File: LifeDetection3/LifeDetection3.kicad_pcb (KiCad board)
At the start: 4 copper layers, 19 parts, among them J1 Power, J13 XT60PW-M, J2 PWM, J3 Analog, J4 PWM, J5 Analog, J6 Communication, J7 Digital

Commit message: lil changes
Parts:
- added ?: , , F.Cu at (196.5, 97.5)
- added ?: , , F.Cu at (163.5, 92.4)
- added ?: , , F.Cu at (114.0, 97.5)
- added ?: , , F.Cu at (115.2, 49.2)
- added P13: CONN_01X01, Socket_Arduino_Mega:Arduino_1pin, F.Cu at (190.2, 49.2)
- moved J13 23.0 mm to (102.5, 46.7)
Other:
- board outline added: 105 x 88.1 mm
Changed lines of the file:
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@@
     )
+  )
+  (footprint "" (layer "F.Cu")
+    (at 196.52 97.485)
+    (fp_text reference "" (at 0 0) (layer "F.SilkS")
+      (effects (font (size 1.27 1.27) (thickness 0.15)))
+    )
+    (fp_text value "" (at 0 0) (layer "F.SilkS")
+      (effects (font (size 1.27 1.27) (thickness 0.15)))
+    )
+    (pad "1" thru_hole circle locked (at 0 0) (size 4.064 4.064) (drill 3.048) (layers *.Mask "F.Cu" "In1.Cu" "In2.Cu" "B.Cu" "F.SilkS")
+      (pinfunction "Pin_1") (pintype "passive+no_connect"))
   )
   (footprint "Connector_PinSocket_2.54mm:PinSocket_1x08_P2.54mm_Vertical" (layer "F.Cu")
@@
     )
   )
+  (footprint "" (layer "F.Cu")
+    (at 163.5 92.38)
+    (fp_text reference "" (at 0 0) (layer "F.SilkS")
+      (effects (font (size 1.27 1.27) (thickness 0.15)))
+    )
+    (fp_text value "" (at 0 0) (layer "F.SilkS")
+      (effects (font (size 1.27 1.27) (thickness 0.15)))
+    )
+    (pad "1" thru_hole circle locked (at 0 0) (size 4.064 4.064) (drill 3.048) (layers *.Mask "F.Cu" "In1.Cu" "In2.Cu" "B.Cu" "F.SilkS")
+      (pinfunction "Pin_1") (pintype "passive+no_connect"))
+  )
   (footprint "XT60:AMASS_XT60PW-M" (layer "F.Cu")
-    (at 105.08 69.52 90)
+    (at 102.54 46.66 90)
     (property "MANUFACTURER" "AMASS")
     (property "MAXIMUM_PACKAGE_HEIGHT" "8.4 mm")
@@
     )
   )
+  (footprint "" (layer "F.Cu")
+    (at 113.97 97.485)
+    (fp_text reference "" (at 0 0) (layer "F.SilkS")
+      (effects (font (size 1.27 1.27) (thickness 0.15)))
+    )
+    (fp_text value "" (at 0 0) (layer "F.SilkS")
+      (effects (font (size 1.27 1.27) (thickness 0.15)))
+    )
+    (pad "1" thru_hole circle locked (at 0 0) (size 4.064 4.064) (drill 3.048) (layers *.Mask "F.Cu" "In1.Cu" "In2.Cu" "B.Cu" "F.SilkS")
+      (pinfunction "Pin_1") (pintype "passive+no_connect"))
+  )
   (footprint "Connector_PinSocket_2.54mm:PinSocket_1x08_P2.54mm_Vertical" (layer "F.Cu")
     (at 171.12 64.44)
@@
     )
   )
+  (footprint "Socket_Arduino_Mega:Arduino_1pin" (layer "F.Cu")
+    (at 190.17 49.225)
+    (descr "module 1 pin (ou trou mecanique de percage)")
+    (tags "DEV")
+    (property "Sheetfile" "ArmSheildR2.kicad_sch")
+    (property "Sheetname" "")
+    (attr through_hole)
+    (fp_text reference "P13" (at 0 -3.048) (layer "F.SilkS") hide
+      (effects (font (size 1 1) (thickness 0.15)))
+    )
+    (fp_text value "CONN_01X01" (at 0 2.794) (layer "F.Fab") hide
+      (effects (font (size 1 1) (thickness 0.15)))
+    )
+    (fp_circle (center 0 0) (end 0 -2.286) (layer "F.SilkS") (width 0.15) (fill none))
+    (pad "1" thru_hole circle locked (at 0 0) (size 4.064 4.064) (drill 3.048) (layers *.Mask "F.Cu" "In1.Cu" "In2.Cu" "B.Cu" "F.SilkS")
+      (pinfunction "Pin_1") (pintype "passive+no_connect"))
+  )
   (footprint "Connector_PinSocket_2.54mm:PinSocket_1x08_P2.54mm_Vertical" (layer "F.Cu")
     (at 155.88 64.44)
@@
     )
   )
-  (gr_rect (start 201.6 110.16) (end 89.84 26.34) (layer "F.Cu") (width 0.15) (fill none))
+  (footprint "" (layer "F.Cu")
+    (at 115.24 49.225)
+    (fp_text reference "" (at 0 0) (layer "F.SilkS")
+      (effects (font (size 1.27 1.27) (thickness 0.15)))
+    )
+    (fp_text value "" (at 0 0) (layer "F.SilkS")
+      (effects (font (size 1.27 1.27) (thickness 0.15)))
+    )
+    (pad "1" thru_hole circle locked (at 0 0) (size 4.064 4.064) (drill 3.048) (layers *.Mask "F.Cu" "In1.Cu" "In2.Cu" "B.Cu" "F.SilkS")
+      (pinfunction "Pin_1") (pintype "passive+no_connect"))
+  )
+  (gr_line (start 94.62 57.02) (end 94.62 46.02) (layer "Edge.Cuts") (width 0.15))
+  (gr_line (start 101.62 23.8) (end 189.62 23.8) (layer "Edge.Cuts") (width 0.15))
+  (gr_arc (start 94.62 80.02) (mid 95.205786 78.605786) (end 96.62 78.02) (layer "Edge.Cuts") (width 0.15))
+  (gr_arc (start 98.62 61.02) (mid 95.791573 59.848427) (end 94.62 57.02) (layer "Edge.Cuts") (width 0.15))
+  (gr_arc (start 199.62 105.917359) (mid 197.862641 110.16) (end 193.62 111.917359) (layer "Edge.Cuts") (width 0.15))
+  (gr_line (start 105.62 61.02) (end 98.62 61.02) (layer "Edge.Cuts") (width 0.15))
+  (gr_line (start 191.44 23.8) (end 189.62 23.8) (layer "Edge.Cuts") (width 0.15))
+  (gr_line (start 199.62 105.917359) (end 199.62 33.02) (layer "Edge.Cuts") (width 0.15))
+  (gr_arc (start 94.62 31.42) (mid 96.643931 26.254034) (end 101.62 23.8) (layer "Edge.Cuts") (width 0.15))
+  (gr_arc (start 101.62 111.917359) (mid 96.670253 109.867106) (end 94.62 104.917359) (layer "Edge.Cuts") (width 0.15))
+  (gr_line (start 199.62 31.42) (end 199.62 33.02) (layer "Edge.Cuts") (width 0.15))
+  (gr_line (start 94.62 46.02) (end 94.62 31.42) (layer "Edge.Cuts") (width 0.15))
+  (gr_arc (start 105.62 61.02) (mid 107.034214 61.605786) (end 107.62 63.02) (layer "Edge.Cuts") (width 0.15))
+  (gr_arc (start 107.62 76.02) (mid 107.034214 77.434214) (end 105.62 78.02) (layer "Edge.Cuts") (width 0.15))
+  (gr_line (start 107.62 63.02) (end 107.62 76.02) (layer "Edge.Cuts") (width 0.15))
+  (gr_line (start 105.62 78.02) (end 96.62 78.02) (layer "Edge.Cuts") (width 0.15))
+  (gr_line (start 94.62 80.02) (end 94.62 104.917359) (layer "Edge.Cuts") (width 0.15))
+  (gr_arc (start 191.44 23.8) (mid 196.911013 26.127496) (end 199.62 31.42) (layer "Edge.Cuts") (width 0.15))
+  (gr_line (start 193.62 111.917359) (end 101.62 111.917359) (layer "Edge.Cuts") (width 0.15))
   (segment (start 171.12 69.52) (end 158.42 82.22) (width 0.25) (layer "F.Cu") (net 1))
   (segment (start 158.42 82.22) (end 155.88 82.22) (width 0.25) (layer "F.Cu") (net 1))

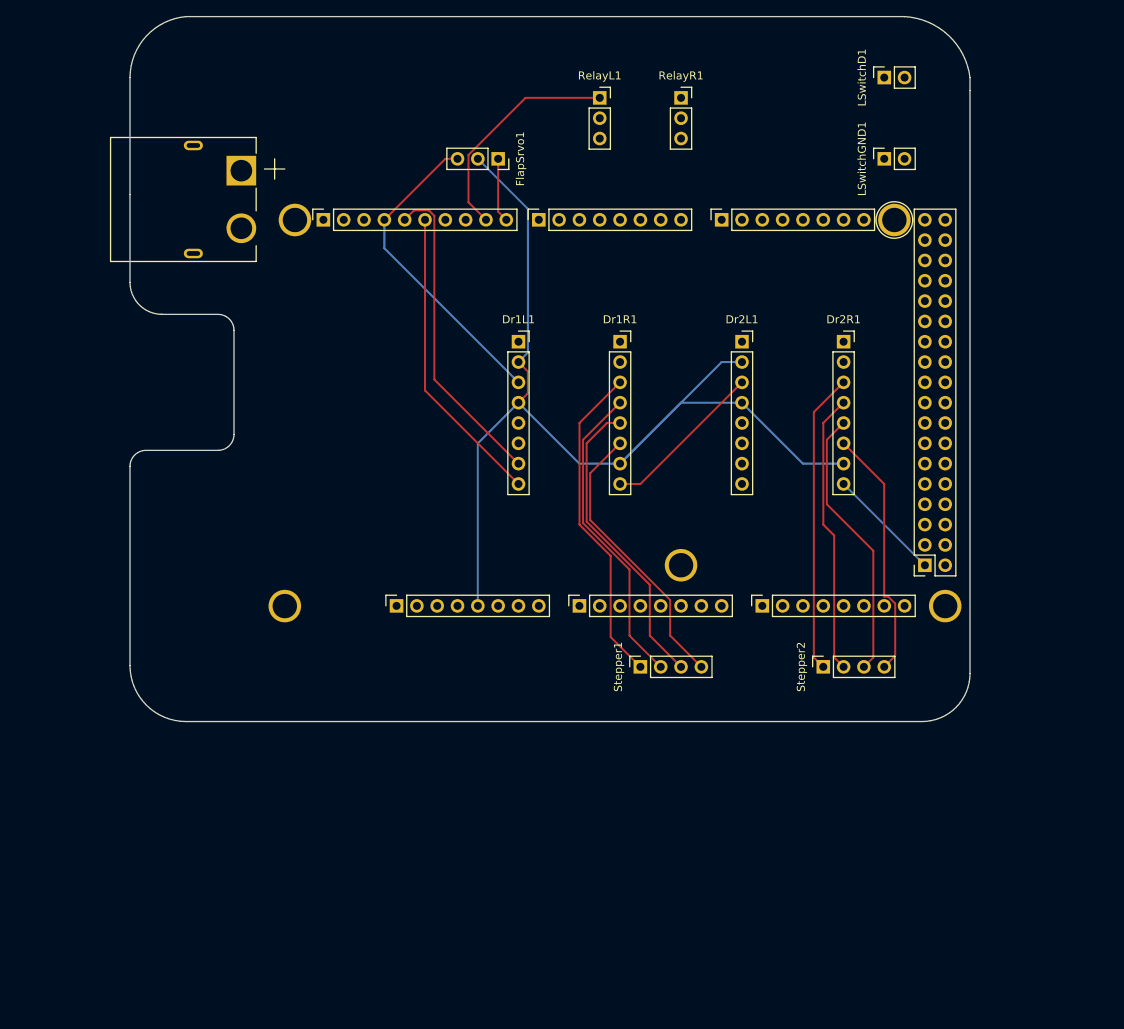
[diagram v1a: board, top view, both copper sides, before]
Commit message: 2 layers + connector footprint
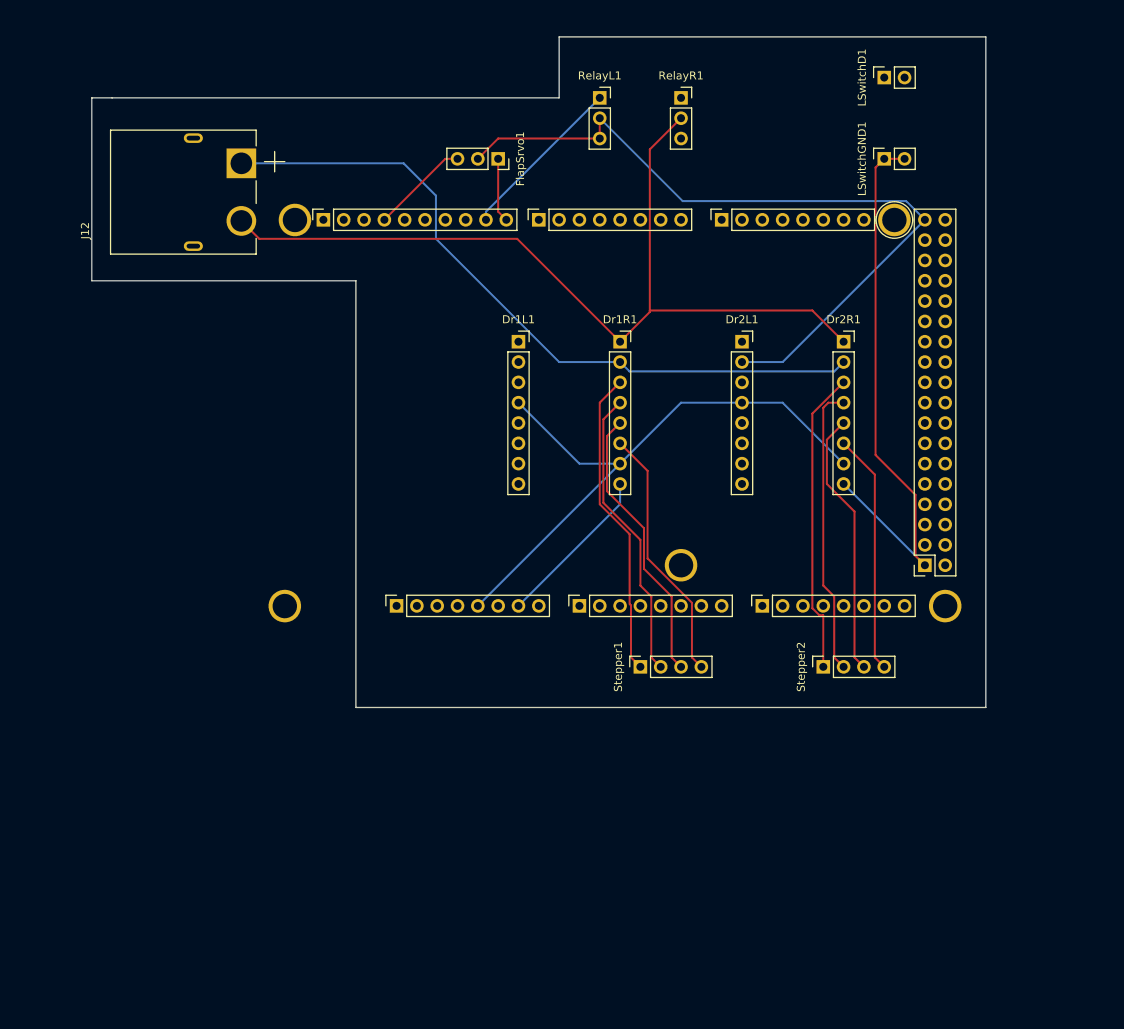
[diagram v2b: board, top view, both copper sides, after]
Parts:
- removed J13: XT60PW-M, XT60:AMASS_XT60PW-M
- added J12: XT60PW-M, XT60PW-M:AMASS_XT60PW-M, F.Cu at (102.5, 45.7)
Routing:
- net Net-(Dr1R1-Pad1): track 0.00 -> 110.5 mm
- net Net-(Dr1R1-Pad2): track 0.00 -> 89.7 mm
- net /*13: track 39.8 -> 0.00 mm
- net /*12: track 37.9 -> 0.00 mm
- net +5V: track 132.6 -> 170.2 mm
- net GND: track 74.4 -> 103.5 mm
- net /*9: track 28.4 -> 21.1 mm
- net Net-(Stepper1-Pad4): track 35.2 -> 32.1 mm
- net Net-(Stepper1-Pad3): track 38.1 -> 35.0 mm
- net Net-(Stepper1-Pad1): track 40.8 -> 38.7 mm
- net Net-(Stepper1-Pad2): track 39.0 -> 36.9 mm
- net Net-(Stepper2-Pad4): track 31.5 -> 30.0 mm
- net Net-(Stepper2-Pad2): track 35.1 -> 36.2 mm
- net Net-(Stepper2-Pad3): track 34.2 -> 33.3 mm
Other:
- board size 105 x 88.1 mm -> 111.8 x 83.8 mm
- copper layers 4 -> 2

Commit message: logo added
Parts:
- added G***: LOGO, Graphics and Logos:uORover20mm, B.Cu at (133.0, 77.1)
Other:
- outline, holes or cut-outs redrawn
- board text added: "Developed 2023"
- board text added: "uORover LDShield Mk1"

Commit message: edge & 3D models
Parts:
- moved G*** 5.08 mm to (127.9, 77.1)
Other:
- board size 111.8 x 83.8 mm -> 101.6 x 83.8 mm
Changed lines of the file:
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@@
       (rotate (xyz 0 0 0))
     )
+    (model "/Users/maximecouture/Downloads/A4988 STEPPER MOTOR DRIVER CARRIER--3DModel-STEP-56544.STEP"
+      (offset (xyz 6.5 -9 7))
+      (scale (xyz 1 1 1))
+      (rotate (xyz -90 0 0))
+    )
   )
   (footprint "Connector_PinSocket_2.54mm:PinSocket_1x03_P2.54mm_Vertical" (layer "F.Cu")
@@
       (rotate (xyz 0 0 0))
     )
+    (model "/Users/maximecouture/Downloads/A4988 STEPPER MOTOR DRIVER CARRIER--3DModel-STEP-56544.STEP"
+      (offset (xyz 6.5 -9 7))
+      (scale (xyz 1 1 1))
+      (rotate (xyz -90 0 0))
+    )
   )
   (footprint "Connector_PinSocket_2.54mm:PinSocket_1x03_P2.54mm_Vertical" (layer "F.Cu")
@@
     (pad "S1" thru_hole oval locked (at 6.75 0 90) (size 1.2 2.4) (drill oval 0.6 1.7) (layers *.Cu *.Mask))
     (pad "S2" thru_hole oval locked (at -6.75 0 90) (size 1.2 2.4) (drill oval 0.6 1.7) (layers *.Cu *.Mask))
+    (model "/Users/maximecouture/Downloads/XT60PW-M--3DModel-STEP-1.STEP"
+      (offset (xyz 0 9.35 3))
+      (scale (xyz 1 1 1))
+      (rotate (xyz -90 0 -180))
+    )
   )
   (footprint "Connector_PinSocket_2.54mm:PinSocket_1x08_P2.54mm_Vertical" (layer "F.Cu")
@@
   )
   (footprint "Graphics and Logos:uORover20mm" (layer "B.Cu")
-    (at 133.02 77.14 180)
+    (at 127.94 77.14 180)
     (attr board_only exclude_from_pos_files exclude_from_bom)
     (fp_text reference "G***" (at 0 0) (layer "B.SilkS") hide
@@
     (pts
       (xy 201.6 110.16)
-      (xy 122.86 110.16)
-      (xy 122.86 56.82)
-      (xy 89.84 56.82)
-      (xy 89.84 33.96)
-      (xy 89.84 33.96)
-      (xy 89.84 26.34)
+      (xy 110.16 110.16)
+      (xy 110.16 56.82)
+      (xy 100 56.82)
+      (xy 100 33.96)
+      (xy 120.32 33.96)
+      (xy 125.4 26.34)
       (xy 148.26 26.34)
       (xy 201.6 26.34)
     ) (layer "Edge.Cuts") (width 0.15) (fill none))
-  (gr_text "Developed 2023" (at 150.8 92.38) (layer "B.SilkS")
+  (gr_text "Developed 2023" (at 145.72 92.38) (layer "B.SilkS")
     (effects (font (size 1 1) (thickness 0.15)) (justify mirror))
   )
-  (gr_text "uORover LDShield Mk1" (at 140.132 89.586) (layer "B.SilkS")
+  (gr_text "uORover LDShield Mk1" (at 135.052 89.586) (layer "B.SilkS")
     (effects (font (size 4 2) (thickness 0.15)) (justify mirror))
   )

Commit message: more tracing
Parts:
- removed ? (x4): , 
- removed P13: CONN_01X01, Socket_Arduino_Mega:Arduino_1pin
- added +Batt1: Conn_01x01, TestPoint:TestPoint_THTPad_D4.0mm_Drill2.0mm, F.Cu at (176.2, 31.4)
- added TempSens1: Conn_01x04, Connector_PinSocket_2.54mm:PinSocket_1x04_P2.54mm_Vertical, F.Cu at (127.9, 105.1)
- G***: moved to F.Cu
- turned G*** to 0 degrees
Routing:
- net GND: track 103.5 -> 163.8 mm, vias 0 -> 2
- net /SDA/20: track 0.00 -> 59.7 mm
- net /SCL/21: track 0.00 -> 59.7 mm
- net /*11: track 0.00 -> 55.7 mm, vias 0 -> 4
- net /*10: track 0.00 -> 54.2 mm, vias 0 -> 2
- net Net-(+Batt1-Pad1): track 89.7 -> 141.5 mm
- net /*12: track 0.00 -> 37.9 mm, vias 0 -> 2
- net +5V: track 170.2 -> 207.0 mm, vias 0 -> 2
- net /*13: track 0.00 -> 36.4 mm
- net +3V3: track 0.00 -> 8.67 mm

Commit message: almost done
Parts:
- removed RelayL1, RelayR1: Conn_01x03, Connector_PinSocket_2.54mm:PinSocket_1x03_P2.54mm_Vertical
- added ?: , , F.Cu at (190.2, 49.2)
- added ?: , , F.Cu at (115.2, 49.2)
- added P10: CONN_01X01, Socket_Arduino_Mega:Arduino_1pin, F.Cu at (196.5, 97.4)
- added P8: CONN_01X01, Socket_Arduino_Mega:Arduino_1pin, F.Cu at (114.0, 97.4)
- added P9: CONN_01X01, Socket_Arduino_Mega:Arduino_1pin, F.Cu at (166.0, 92.3)
- added U1: TLP3545, Package_DIP:DIP-6_W7.62mm, F.Cu at (166.0, 39.0)
- added VacuumGND1: Conn_01x01, TestPoint:TestPoint_THTPad_D4.0mm_Drill2.0mm, F.Cu at (176.2, 39.0)
- renumbered +Batt1 to Vacuum+1
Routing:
- net /48: track 0.00 -> 60.2 mm
- net /47: track 0.00 -> 55.4 mm
- net GND: track 163.8 -> 188.7 mm
- net +5V: track 207.0 -> 221.2 mm, vias 2 -> 3
- net Net-(U1-Pad1): track 0.00 -> 10.2 mm
- net /*9: track 21.1 -> 25.6 mm
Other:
- outline, holes or cut-outs redrawn

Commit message: final touches
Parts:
- moved J1 38.7 mm to (143.2, 133.0)
- moved J5 38.7 mm to (188.9, 133.0)
- moved P10 38.7 mm to (211.7, 133.0)
- moved P8 38.7 mm to (129.2, 133.0)
- moved J3 38.7 mm to (166.0, 133.0)
- moved Dr1R1 38.7 mm to (171.1, 100.0)
- moved Dr2L1 38.7 mm to (186.4, 100.0)
- moved Dr2R1 38.7 mm to (199.1, 100.0)
- moved FlapSrvo1 38.7 mm to (155.9, 77.1)
- moved G*** 38.7 mm to (143.2, 112.7)
- moved J2 38.7 mm to (134.0, 84.8)
- moved J4 38.7 mm to (161.0, 84.8)
- moved J7 38.7 mm to (209.2, 127.9)
- moved Vacuum+1 38.7 mm to (191.4, 67.0)
- moved ? 38.7 mm to (130.5, 84.7)
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
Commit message: final touches
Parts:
- moved Stepper2 23.0 mm to (173.7, 143.2)
- moved TempSens1 23.0 mm to (120.3, 143.2)
- moved ? 23.0 mm to (107.6, 87.3)
- moved Dr1R1 23.0 mm to (148.3, 102.5)
- moved Dr2L1 23.0 mm to (163.5, 102.5)
- moved Dr2R1 23.0 mm to (176.2, 102.5)
- moved G*** 23.0 mm to (120.3, 115.2)
- moved J1 23.0 mm to (120.3, 135.6)
- moved J4 23.0 mm to (138.1, 87.3)
- moved J5 23.0 mm to (166.0, 135.6)
- moved P10 23.0 mm to (188.9, 135.5)
- moved U1 23.0 mm to (158.4, 77.1)
- moved J12 23.0 mm to (94.9, 83.8)
- moved J2 23.0 mm to (111.2, 87.3)
- moved P8 23.0 mm to (106.3, 135.5)
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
